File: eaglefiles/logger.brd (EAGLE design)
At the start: 43.2 x 20 mm, 38 parts, among them K1 65100516121, Q2 IRLML9301, U1 MCP1640, U3 FT232RLSSOP

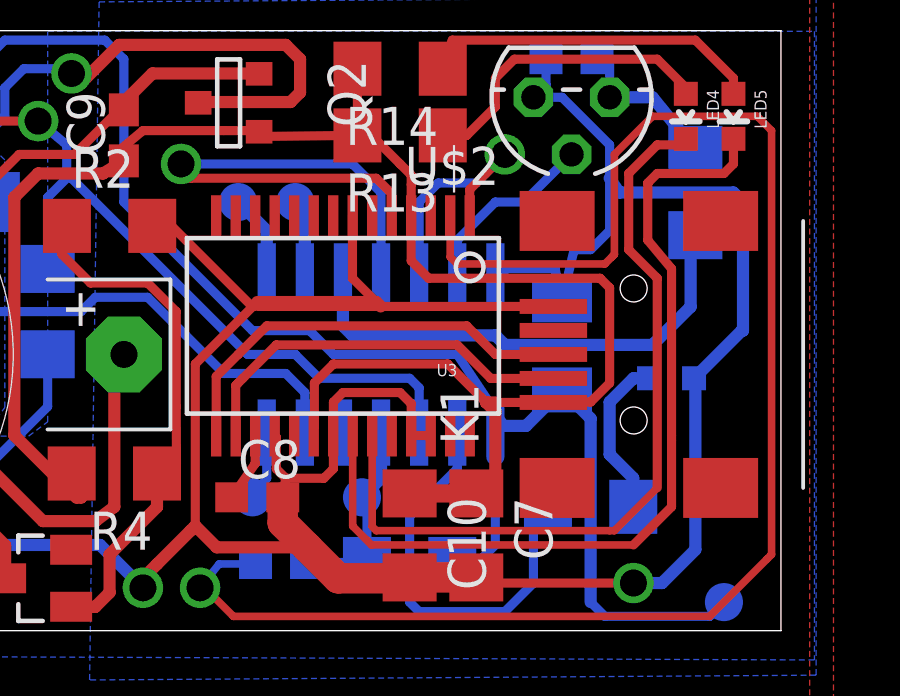
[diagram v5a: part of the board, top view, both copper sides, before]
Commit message: Adjusted reverse voltage of uart -> FT232 VCC
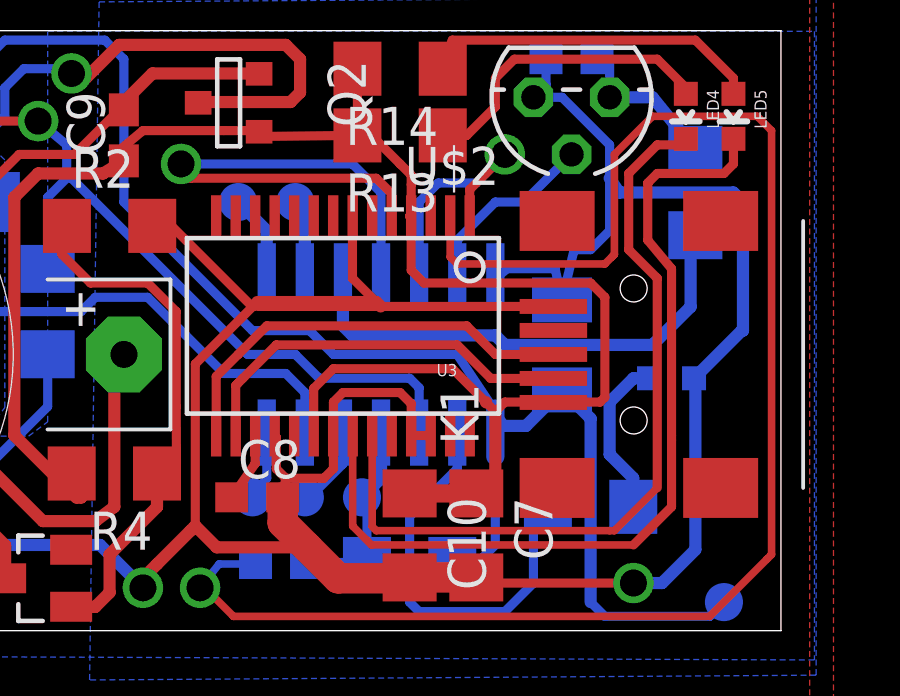
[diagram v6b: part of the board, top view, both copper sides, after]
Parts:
- added U$13: (no value), 0liver:PIN-1.27
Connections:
- new net CK: IC1.5, U$13.P$1
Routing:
- net CK: track 0.00 -> 2.78 mm
- net V_USB: track 61.5 -> 60.8 mm
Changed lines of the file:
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@@
 <element name="D3" library="diode" package="SOT23" value="PMEG2010AET" x="18.415" y="1.74625" rot="R90"/>
 <element name="R8" library="resistor" package="R1206" value="68k" x="18.7325" y="10.63625" rot="MR90"/>
+<element name="U$13" library="0liver" package="PIN-1.27" value="" x="27.305" y="4.445" rot="MR0"/>
 </elements>
 <signals>
@@
 </signal>
 <signal name="V_USB">
-<contactref element="U3" pad="20"/>
 <contactref element="C7" pad="1"/>
-<contactref element="U3" pad="4"/>
 <contactref element="R14" pad="2"/>
 <contactref element="R13" pad="2"/>
 <contactref element="K1" pad="1"/>
 <contactref element="Q2" pad="3"/>
-<wire x1="35.59" y1="7.6075" x2="33.655" y2="7.6075" width="0.3048" layer="1"/>
-<wire x1="33.655" y1="7.6075" x2="33.35" y2="7.6075" width="0.3048" layer="1"/>
-<wire x1="33.35" y1="7.6075" x2="33.3375" y2="7.62" width="0.3048" layer="1"/>
-<wire x1="33.3375" y1="7.62" x2="33.17875" y2="7.77875" width="0.3048" layer="1"/>
-<wire x1="33.17875" y1="7.77875" x2="32.0675" y2="8.89" width="0.3048" layer="1"/>
-<wire x1="32.0675" y1="8.89" x2="28.2575" y2="8.89" width="0.3048" layer="1"/>
-<wire x1="28.2575" y1="8.89" x2="27.6225" y2="8.255" width="0.3048" layer="1"/>
-<wire x1="27.6225" y1="8.255" x2="27.6225" y2="7.1615" width="0.3048" layer="1"/>
-<wire x1="27.6225" y1="7.1615" x2="27.6" y2="6.504" width="0.3048" layer="1"/>
 <wire x1="35.6025" y1="7.62" x2="35.59" y2="7.6075" width="0.3048" layer="1"/>
-<wire x1="30.85" y1="13.816" x2="30.85" y2="12.33" width="0.3048" layer="1"/>
-<wire x1="30.85" y1="12.33" x2="31.4325" y2="11.7475" width="0.3048" layer="1"/>
-<wire x1="31.4325" y1="11.7475" x2="37.1475" y2="11.7475" width="0.3048" layer="1"/>
-<wire x1="37.1475" y1="11.7475" x2="37.465" y2="11.43" width="0.3048" layer="1"/>
 <contactref element="C9" pad="1"/>
 <contactref element="R4" pad="2"/>
-<wire x1="35.6025" y1="7.62" x2="36.83" y2="7.62" width="0.3048" layer="1"/>
-<wire x1="36.83" y1="7.62" x2="37.465" y2="8.255" width="0.3048" layer="1"/>
-<wire x1="37.465" y1="8.255" x2="37.465" y2="11.43" width="0.3048" layer="1"/>
 <wire x1="25.781" y1="16.63065" x2="25.68615" y2="16.4719" width="0.3048" layer="1"/>
 <wire x1="25.68615" y1="16.4719" x2="29.058" y2="16.51" width="0.3048" layer="1"/>
 <wire x1="29.058" y1="16.51" x2="29.5275" y2="16.51" width="0.3048" layer="1"/>
 <wire x1="29.5275" y1="16.51" x2="30.48" y2="15.5575" width="0.3048" layer="1"/>
-<wire x1="30.85" y1="13.816" x2="30.85" y2="14.87" width="0.3048" layer="1"/>
 <wire x1="29.058" y1="18.7325" x2="29.058" y2="16.51" width="0.3048" layer="1"/>
 <wire x1="25.781" y1="16.63065" x2="25.83815" y2="16.63065" width="0.3048" layer="1"/>
@@
 <contactref element="C10" pad="1"/>
 <wire x1="30.7975" y1="4.575" x2="33.02" y2="4.575" width="0.6096" layer="1"/>
-<wire x1="33.655" y1="7.6075" x2="33.35" y2="7.6075" width="0.4064" layer="1"/>
 <wire x1="33.35" y1="7.6075" x2="33.3375" y2="7.62" width="0.4064" layer="1"/>
-<wire x1="33.3375" y1="7.62" x2="33.655" y2="7.3025" width="0.4064" layer="1"/>
 <wire x1="33.655" y1="7.3025" x2="33.655" y2="5.21" width="0.4064" layer="1"/>
 <wire x1="33.655" y1="5.21" x2="33.02" y2="4.575" width="0.4064" layer="1"/>
@@
 <wire x1="30.48" y1="15.5575" x2="30.85" y2="15.1875" width="0.3048" layer="1"/>
 <wire x1="30.85" y1="15.1875" x2="30.85" y2="14.87" width="0.3048" layer="1"/>
+<contactref element="U3" pad="20"/>
+<contactref element="U3" pad="4"/>
+<wire x1="30.85" y1="13.816" x2="30.7975" y2="13.816" width="0.3048" layer="1"/>
+<wire x1="30.7975" y1="13.816" x2="30.7975" y2="13.81125" width="0.3048" layer="1"/>
+<wire x1="30.85" y1="14.87" x2="30.85" y2="13.816" width="0.3048" layer="1"/>
+<wire x1="30.85" y1="13.816" x2="30.85" y2="12.0125" width="0.3048" layer="1"/>
+<wire x1="30.85" y1="12.0125" x2="31.27375" y2="11.58875" width="0.3048" layer="1"/>
+<wire x1="31.27375" y1="11.58875" x2="36.83" y2="11.58875" width="0.3048" layer="1"/>
+<wire x1="36.83" y1="11.58875" x2="37.30625" y2="11.1125" width="0.3048" layer="1"/>
+<wire x1="37.30625" y1="11.1125" x2="37.30625" y2="7.77875" width="0.3048" layer="1"/>
+<wire x1="37.30625" y1="7.77875" x2="37.1475" y2="7.62" width="0.3048" layer="1"/>
+<wire x1="37.1475" y1="7.62" x2="33.9725" y2="7.62" width="0.3048" layer="1"/>
+<wire x1="33.9725" y1="7.62" x2="33.655" y2="7.3025" width="0.3048" layer="1"/>
+<wire x1="33.655" y1="7.3025" x2="33.35" y2="7.6075" width="0.3048" layer="1"/>
+<wire x1="27.6" y1="6.504" x2="27.6" y2="8.07375" width="0.3048" layer="1"/>
+<wire x1="27.6" y1="8.07375" x2="28.2575" y2="8.73125" width="0.3048" layer="1"/>
+<wire x1="28.2575" y1="8.73125" x2="32.22625" y2="8.73125" width="0.3048" layer="1"/>
+<wire x1="32.22625" y1="8.73125" x2="33.3375" y2="7.62" width="0.3048" layer="1"/>
+<wire x1="37.1475" y1="7.62" x2="35.59" y2="7.6075" width="0" layer="19" extent="1-1"/>
 </signal>
 <signal name="N$3">
@@
 <wire x1="18.7325" y1="14.44625" x2="19.446875" y2="15.160625" width="0.3048" layer="16"/>
 </signal>
+<signal name="CK">
+<contactref element="IC1" pad="5"/>
+<contactref element="U$13" pad="P$1"/>
+<wire x1="27.305" y1="4.445" x2="27.46375" y2="4.445" width="0.3048" layer="16"/>
+<wire x1="27.46375" y1="4.445" x2="28.575" y2="5.55625" width="0.3048" layer="16"/>
+<wire x1="28.575" y1="5.55625" x2="28.575" y2="6.604" width="0.3048" layer="16"/>
+</signal>
 </signals>

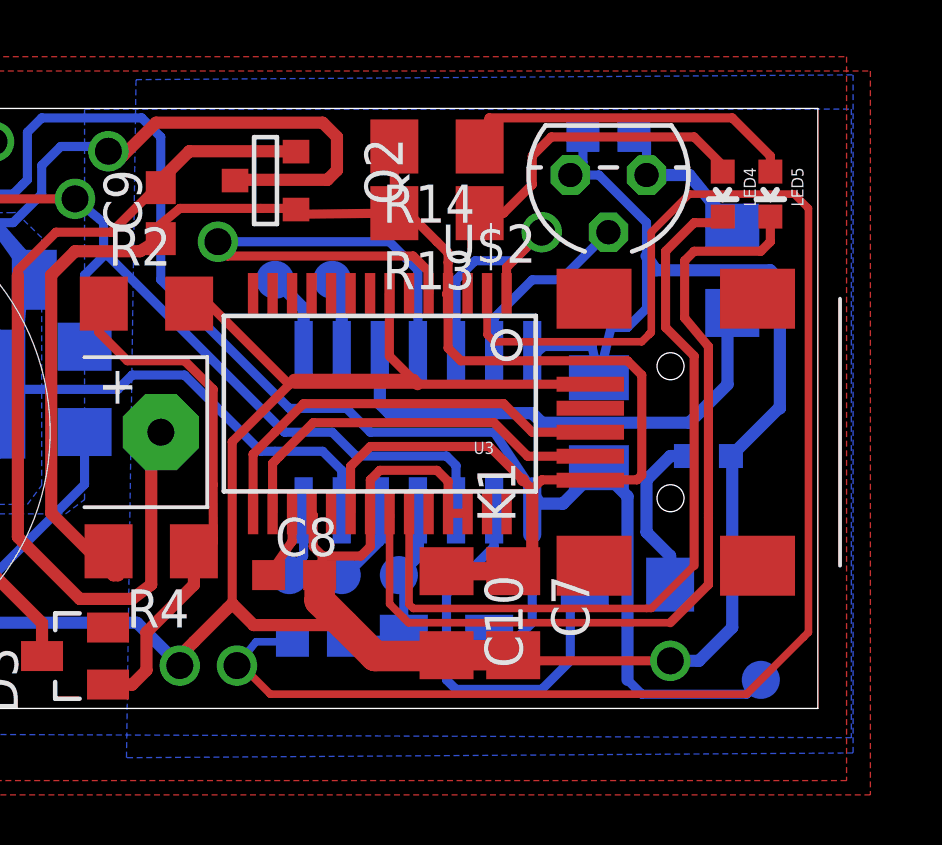
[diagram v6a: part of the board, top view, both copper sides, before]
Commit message: Fixed failure in schematic: TX and RX mixed up...
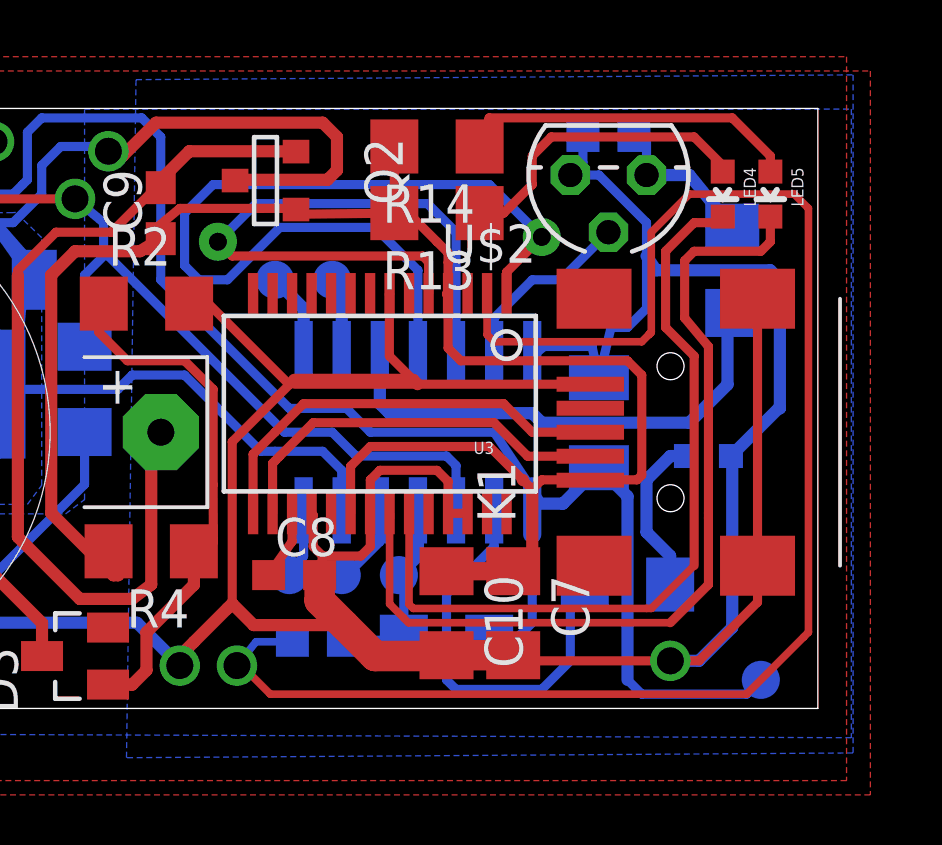
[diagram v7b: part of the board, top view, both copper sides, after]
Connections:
- net GND: now also K1.Z3, K1.Z4
- net N$1: now also U3.1; no longer U3.5
- net N$32: now also U3.5; no longer U3.1
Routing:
- net GND: track 160.5 -> 174.3 mm
- net N$32: track 8.54 -> 21.5 mm
- net N$1: track 18.1 -> 29.2 mm

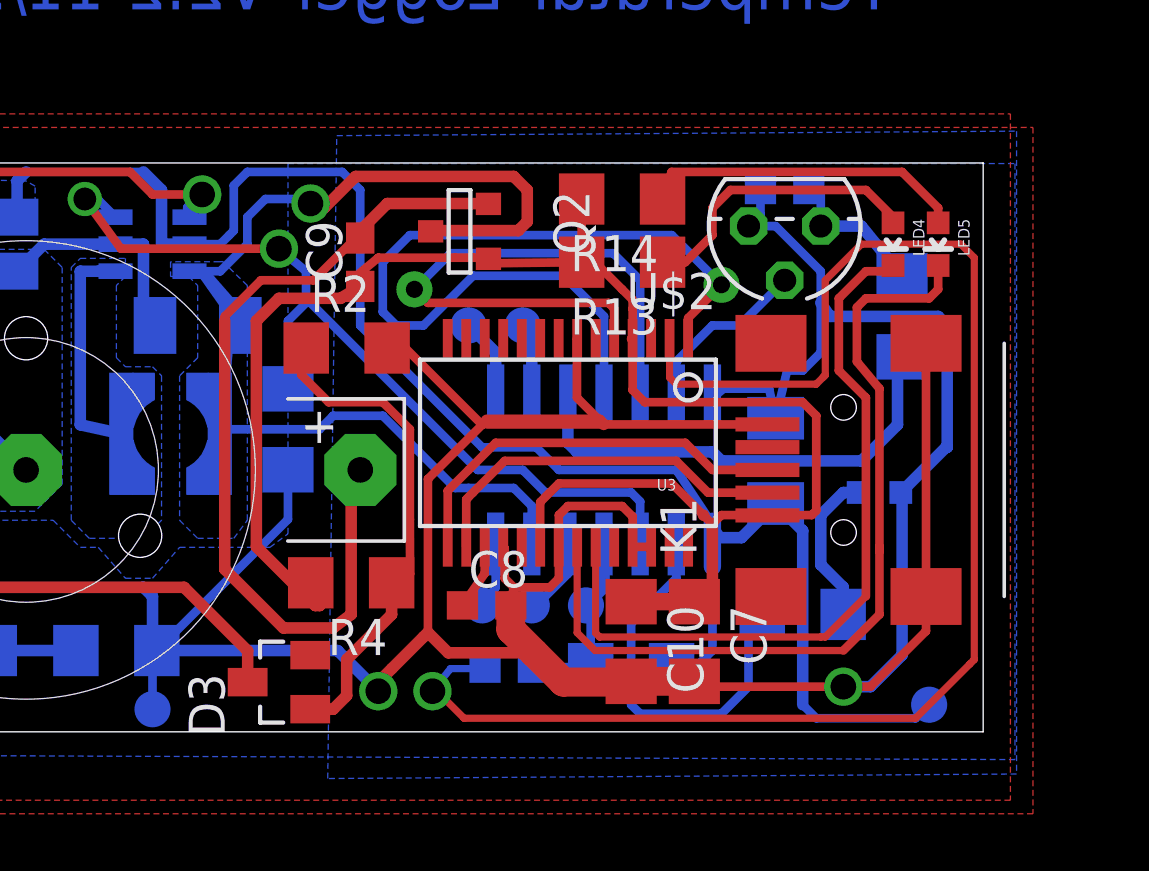
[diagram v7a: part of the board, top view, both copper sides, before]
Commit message: Fixed wrong signal
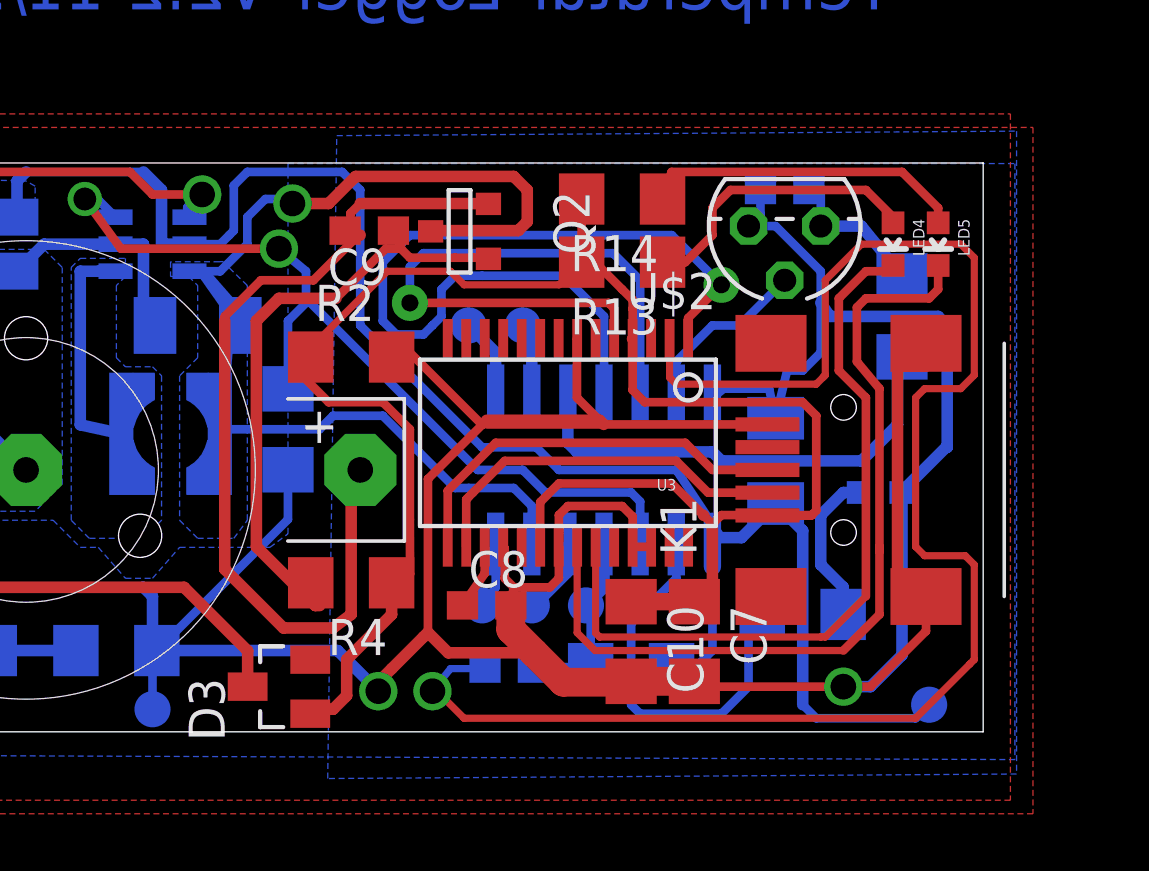
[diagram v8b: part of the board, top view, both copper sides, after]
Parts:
- moved C9 1.16 mm to (21.6, 17.6), turned to 180 degrees
- moved R2 0.35 mm to (21.0, 13.2)
- moved D3 0.16 mm to (18.4, 1.59)
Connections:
- removed net 5V: D3.1, R2.1, R4.1
- new net BATOFF: C9.1, Q2.3, R4.2
- net V_USB: now also D3.1, R2.1, R4.1; no longer C9.1, Q2.3, R4.2
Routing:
- net BATOFF: track 0.00 -> 21.9 mm
- net 5V: track 17.8 -> 0.00 mm
- net V_USB: track 60.8 -> 66.9 mm
- net N$8: track 53.1 -> 56.4 mm
- net GND: track 174.3 -> 176.5 mm
- net N$1: track 29.2 -> 30.2 mm
- net N$32: track 21.5 -> 22.4 mm
- net N$6: track 31.6 -> 32.5 mm
